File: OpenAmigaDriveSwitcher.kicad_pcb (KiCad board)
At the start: 2 copper layers, 21.8 x 57.7 mm, 6 parts, among them J1 SWITCH, J99 OSHW_LOGO, U1 74LS157, U8 EVEN_CIA_CHIP

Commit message: Ready for V1
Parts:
- added J2: SWITCH, OpenAmigaDriveSwitcher:SolderJumper3, F.Cu at (163.3, 106.7)
- J1: footprint OpenAmigaDriveSwitcher:LoosePads-3 -> OpenAmigaDriveSwitcher:Pin_Header_Straight_1x03-ModSilkS
- moved J1 25.1 mm to (163.3, 134.6), turned to 0 degrees
- moved J99 0.77 mm to (150.7, 109.2), turned to 270 degrees
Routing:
- net GND: track 0.00 -> 101.8 mm, vias 0 -> 18
- net VCC: track 46.0 -> 96.1 mm
- net Net-(J1-Pad2): track 28.4 -> 57.9 mm
- net Net-(U1-Pad2): track 16.2 -> 15.3 mm
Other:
- board size 21.8 x 57.7 mm -> 25.1 x 52.3 mm
- net class Power: via_dia 0.6 -> 0.8; via_drill 0.4 -> 0.6
- board text added: "NORMAL"
- board text added: "SWAP"
- board text added: "VCC|SWAP|GND"
- board text added: "github.com/SukkoPera/OpenAmigaDriveSwitcher"

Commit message: Add version number
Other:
- board text added: "V1"
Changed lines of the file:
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@@
     (links 59)
     (no_connects 0)
-    (area 134.62 96.36 178.03 170.086001)
+    (area 140.386999 102.032999 165.683001 154.507001)
     (thickness 1.6)
-    (drawings 23)
+    (drawings 24)
     (tracks 165)
     (zones 0)
@@
     )
   )
+  (gr_text V1 (at 164.084 104.013 90) (layer B.SilkS)
+    (effects (font (size 1 1) (thickness 0.15)) (justify mirror))
+  )
   (gr_text github.com/SukkoPera/OpenAmigaDriveSwitcher (at 151.13 132.842 90) (layer B.SilkS)

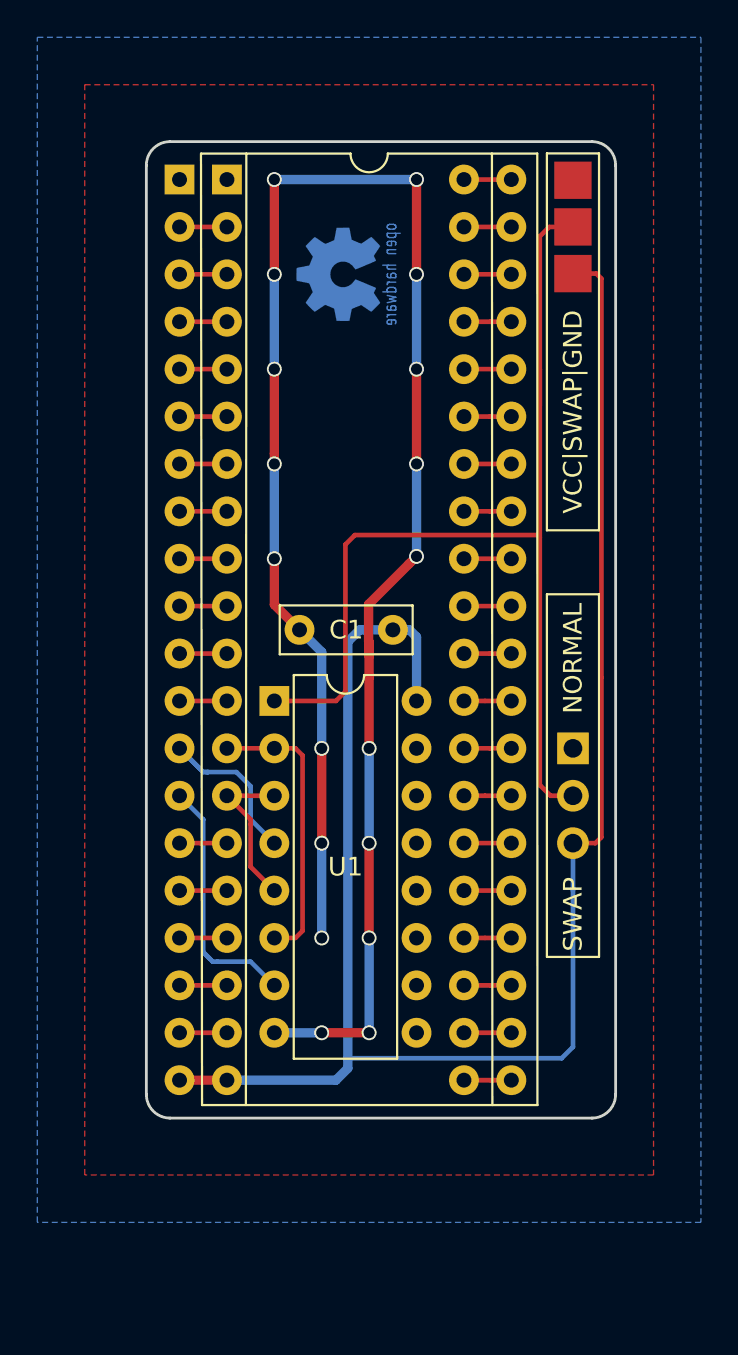
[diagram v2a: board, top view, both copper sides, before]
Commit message: V2: Reverse swap pin logic (i.e: swap drives when it is grounded) This will make the switcher more easily controllable by OpenAmigaMouseTrigger. Also migrate project to KiCad 5.
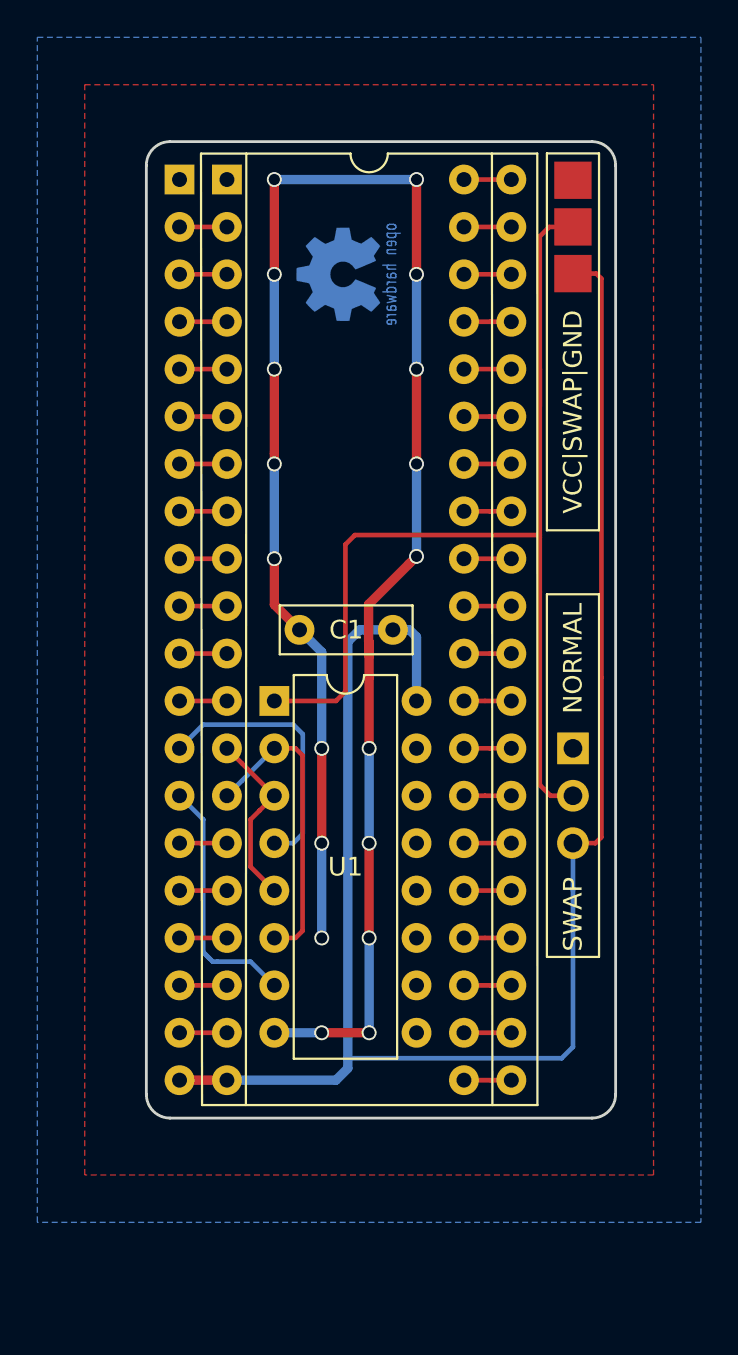
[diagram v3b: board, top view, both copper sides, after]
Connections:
- U8 pad 13: Net-(U1-Pad2) -> Net-(U1-Pad3)
- U8 pad 14: Net-(U1-Pad3) -> Net-(U1-Pad2)
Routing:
- net Net-(CONN1-Pad13): track 9.38 -> 14.4 mm
- net Net-(U1-Pad2): track 15.3 -> 16.3 mm
- net Net-(U1-Pad3): track 8.67 -> 9.72 mm
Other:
- board text added: "V2"
- board text removed: "V1"

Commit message: Remove legacy KiCad 4 symbols
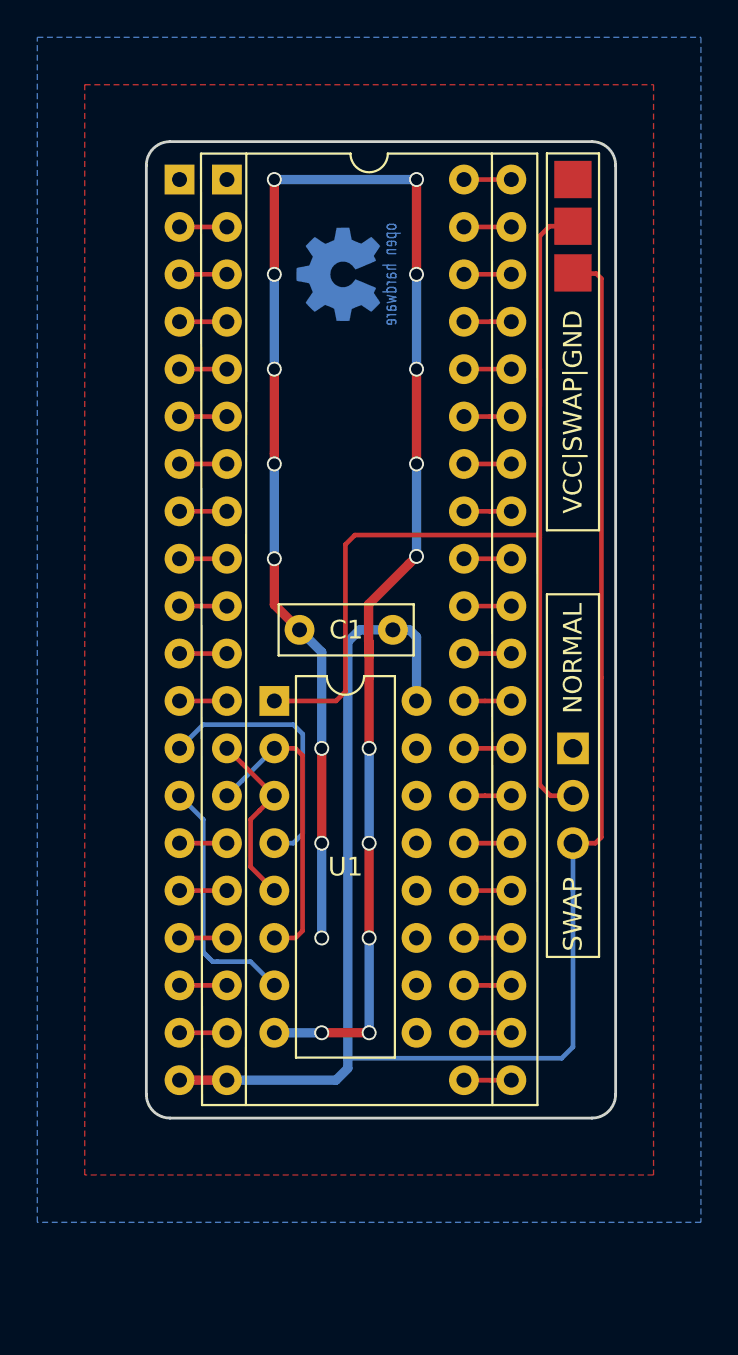
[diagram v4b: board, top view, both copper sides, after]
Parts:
- C1: value C -> 100n; footprint Capacitors_THT:C_Disc_D7.0mm_W2.5mm_P5.00mm -> Capacitor_THT:C_Disc_D7.0mm_W2.5mm_P5.00mm
- J1: value SWITCH -> PADS; footprint OpenAmigaDriveSwitcher:Pin_Header_Straight_1x03-ModSilkS -> OpenAmigaDriveSwitcher:SolderJumper3
- J2: footprint OpenAmigaDriveSwitcher:SolderJumper3 -> OpenAmigaDriveSwitcher:Pin_Header_Straight_1x03-ModSilkS
- U1: footprint Housings_DIP:DIP-16_W7.62mm -> Package_DIP:DIP-16_W7.62mm
- moved J1 28.0 mm to (163.3, 106.6), turned to 270 degrees
- moved J2 27.9 mm to (163.3, 134.6), turned to 0 degrees

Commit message: Fix and improve silkscreen
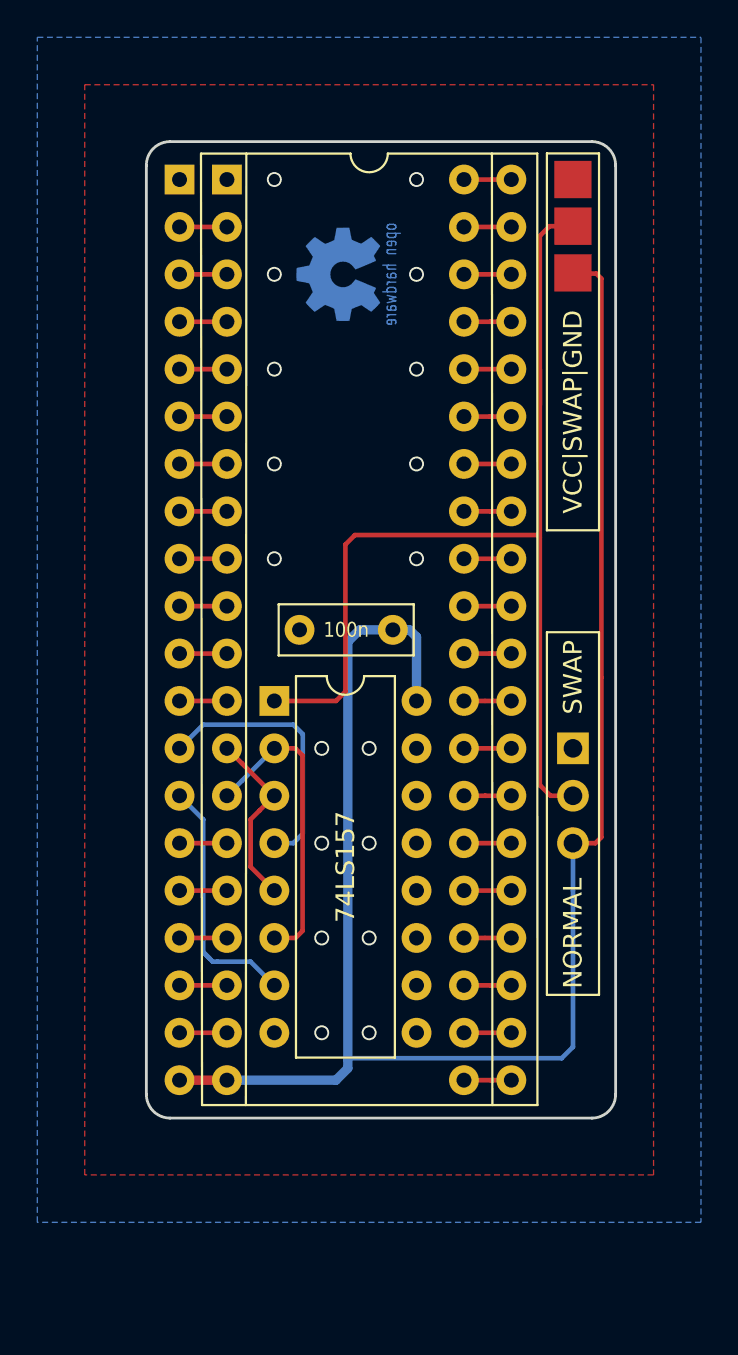
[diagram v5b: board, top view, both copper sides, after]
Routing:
- net GND: track 101.8 -> 0.00 mm
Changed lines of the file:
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@@
     (thickness 1.6)
     (drawings 24)
-    (tracks 161)
+    (tracks 131)
     (zones 0)
     (modules 7)
@@
     (descr "C, Disc series, Radial, pin pitch=5.00mm, , diameter*width=7*2.5mm^2, Capacitor, http://cdn-reichelt.de/documents/datenblatt/B300/DS_KERKO_TC.pdf")
     (tags "C Disc series Radial pin pitch 5.00mm  diameter 7mm width 2.5mm Capacitor")
-    (fp_text reference C1 (at 2.5 0 180) (layer F.SilkS)
-      (effects (font (size 1 1) (thickness 0.15)))
-    )
-    (fp_text value 100n (at 2.5 2.56 180) (layer F.Fab)
-      (effects (font (size 1 1) (thickness 0.15)))
+    (fp_text reference C1 (at 2.5 0 180) (layer F.SilkS) hide
+      (effects (font (size 1 1) (thickness 0.15)))
+    )
+    (fp_text value 100n (at 2.5 0 180) (layer F.SilkS)
+      (effects (font (size 0.8 0.7) (thickness 0.1)))
     )
     (fp_line (start -1 -1.25) (end -1 1.25) (layer F.Fab) (width 0.1))
@@
     (descr "16-lead though-hole mounted DIP package, row spacing 7.62 mm (300 mils)")
     (tags "THT DIP DIL PDIP 2.54mm 7.62mm 300mil")
-    (fp_text reference U1 (at 3.81 8.89) (layer F.SilkS)
-      (effects (font (size 1 1) (thickness 0.15)))
-    )
-    (fp_text value 74LS157 (at 3.81 20.17) (layer F.Fab)
+    (fp_text reference U1 (at 3.81 8.89) (layer F.SilkS) hide
+      (effects (font (size 1 1) (thickness 0.15)))
+    )
+    (fp_text value 74LS157 (at 3.81 8.89 90) (layer F.SilkS)
       (effects (font (size 1 1) (thickness 0.15)))
     )
@@
     (effects (font (size 1 1) (thickness 0.15)) (justify mirror))
   )
-  (gr_line (start 164.719 126.365) (end 164.719 145.796) (layer F.SilkS) (width 0.12))
-  (gr_line (start 161.925 145.796) (end 161.925 126.365) (layer F.SilkS) (width 0.12))
-  (gr_line (start 161.925 145.796) (end 164.719 145.796) (layer F.SilkS) (width 0.12))
-  (gr_line (start 161.925 126.365) (end 164.719 126.365) (layer F.SilkS) (width 0.12))
+  (gr_line (start 164.719 128.397) (end 164.719 147.828) (layer F.SilkS) (width 0.12))
+  (gr_line (start 161.925 147.828) (end 161.925 128.397) (layer F.SilkS) (width 0.12))
+  (gr_line (start 161.925 147.828) (end 164.719 147.828) (layer F.SilkS) (width 0.12))
+  (gr_line (start 161.925 128.397) (end 164.719 128.397) (layer F.SilkS) (width 0.12))
   (gr_line (start 161.925 122.936) (end 164.719 122.936) (layer F.SilkS) (width 0.12))
   (gr_line (start 161.925 102.743) (end 164.719 102.743) (layer F.SilkS) (width 0.12))
@@
     (effects (font (size 1 1) (thickness 0.15)))
   )
-  (gr_text NORMAL (at 163.322 129.794 90) (layer F.SilkS)
+  (gr_text NORMAL (at 163.322 144.526 90) (layer F.SilkS)
     (effects (font (size 1 1) (thickness 0.15)))
   )
-  (gr_text SWAP (at 163.322 143.51 90) (layer F.SilkS)
+  (gr_text SWAP (at 163.322 130.81 90) (layer F.SilkS)
     (effects (font (size 1 1) (thickness 0.15)))
   )
@@
   (gr_line (start 165.608 103.378) (end 165.608 153.162) (layer Edge.Cuts) (width 0.15))
   (gr_line (start 141.732 102.108) (end 164.338 102.108) (layer Edge.Cuts) (width 0.15))
+  (via (at 147.32 104.14) (size 0.8) (drill 0.6) (layers F.Cu B.Cu) (net 2))
   (segment (start 151.257 151.765) (end 151.257 151.257) (width 0.5) (layer B.Cu) (net 1))
   (segment (start 151.257 151.257) (end 151.257 128.905) (width 0.5) (layer B.Cu) (net 1))
@@
   (segment (start 164.572 109.18) (end 164.846 109.454) (width 0.25) (layer F.Cu) (net 1))
   (segment (start 142.24 152.4) (end 144.78 152.4) (width 0.5) (layer F.Cu) (net 1) (status 30))
-  (segment (start 147.32 124.46) (end 147.32 126.92) (width 0.5) (layer F.Cu) (net 2))
-  (segment (start 147.32 126.92) (end 148.67 128.27) (width 0.5) (layer F.Cu) (net 2) (status 20))
-  (segment (start 149.86 134.62) (end 149.86 129.46) (width 0.5) (layer B.Cu) (net 2))
-  (segment (start 149.86 129.46) (end 148.67 128.27) (width 0.5) (layer B.Cu) (net 2) (status 20))
-  (segment (start 147.32 119.38) (end 147.32 118.814315) (width 0.5) (layer F.Cu) (net 2))
-  (segment (start 147.32 118.814315) (end 147.32 114.3) (width 0.5) (layer F.Cu) (net 2))
-  (segment (start 147.32 124.46) (end 147.32 119.38) (width 0.5) (layer B.Cu) (net 2))
-  (via (at 147.32 119.38) (size 0.8) (drill 0.6) (layers F.Cu B.Cu) (net 2))
   (via (at 147.32 124.46) (size 0.8) (drill 0.6) (layers F.Cu B.Cu) (net 2))
-  (segment (start 152.4 129.667) (end 152.4 128.924002) (width 0.5) (layer F.Cu) (net 2))
-  (segment (start 152.4 128.924002) (end 152.369999 128.894001) (width 0.5) (layer F.Cu) (net 2))
-  (segment (start 152.369999 128.894001) (end 152.369999 126.903001) (width 0.5) (layer F.Cu) (net 2))
-  (segment (start 152.369999 126.903001) (end 154.540001 124.732999) (width 0.5) (layer F.Cu) (net 2))
-  (segment (start 154.540001 124.732999) (end 154.94 124.333) (width 0.5) (layer F.Cu) (net 2))
-  (segment (start 154.94 119.38) (end 154.94 124.333) (width 0.5) (layer B.Cu) (net 2))
-  (via (at 154.94 124.333) (size 0.8) (drill 0.6) (layers F.Cu B.Cu) (net 2))
-  (segment (start 154.94 114.3) (end 154.94 119.38) (width 0.5) (layer F.Cu) (net 2))
-  (via (at 154.94 119.38) (size 0.8) (drill 0.6) (layers F.Cu B.Cu) (net 2))
-  (segment (start 154.94 109.22) (end 154.94 114.3) (width 0.5) (layer B.Cu) (net 2))
-  (via (at 154.94 114.3) (size 0.8) (drill 0.6) (layers F.Cu B.Cu) (net 2))
-  (segment (start 154.94 104.14) (end 154.94 109.22) (width 0.5) (layer F.Cu) (net 2))
-  (via (at 154.94 109.22) (size 0.8) (drill 0.6) (layers F.Cu B.Cu) (net 2))
-  (segment (start 147.32 104.14) (end 154.94 104.14) (width 0.5) (layer B.Cu) (net 2))
-  (via (at 154.94 104.14) (size 0.8) (drill 0.6) (layers F.Cu B.Cu) (net 2))
-  (segment (start 147.32 109.22) (end 147.32 104.14) (width 0.5) (layer F.Cu) (net 2))
-  (via (at 147.32 104.14) (size 0.8) (drill 0.6) (layers F.Cu B.Cu) (net 2))
-  (segment (start 147.32 114.3) (end 147.32 109.22) (width 0.5) (layer B.Cu) (net 2))
-  (via (at 147.32 109.22) (size 0.8) (drill 0.6) (layers F.Cu B.Cu) (net 2))
-  (via (at 147.32 114.3) (size 0.8) (drill 0.6) (layers F.Cu B.Cu) (net 2))
-  (segment (start 152.4 129.101315) (end 152.4 129.667) (width 0.5) (layer F.Cu) (net 2))
-  (segment (start 152.369999 129.071314) (end 152.4 129.101315) (width 0.5) (layer F.Cu) (net 2))
-  (segment (start 152.4 130.81) (end 152.4 129.667) (width 0.5) (layer F.Cu) (net 2))
+  (via (at 149.86 149.86) (size 0.8) (drill 0.6) (layers F.Cu B.Cu) (net 2))
+  (via (at 152.4 149.86) (size 0.8) (drill 0.6) (layers F.Cu B.Cu) (net 2))
+  (via (at 152.4 139.7) (size 0.8) (drill 0.6) (layers F.Cu B.Cu) (net 2))
+  (via (at 152.4 134.62) (size 0.8) (drill 0.6) (layers F.Cu B.Cu) (net 2))
   (via (at 149.86 144.78) (size 0.8) (drill 0.6) (layers F.Cu B.Cu) (net 2))
-  (segment (start 149.86 139.7) (end 149.86 144.78) (width 0.5) (layer B.Cu) (net 2))
-  (segment (start 149.86 134.62) (end 149.86 139.7) (width 0.5) (layer F.Cu) (net 2))
   (via (at 149.86 139.7) (size 0.8) (drill 0.6) (layers F.Cu B.Cu) (net 2))
   (via (at 149.86 134.62) (size 0.8) (drill 0.6) (layers F.Cu B.Cu) (net 2))
-  (segment (start 152.4 134.62) (end 152.4 130.81) (width 0.5) (layer F.Cu) (net 2))
-  (segment (start 152.4 139.7) (end 152.4 134.62) (width 0.5) (layer B.Cu) (net 2))
-  (via (at 152.4 134.62) (size 0.8) (drill 0.6) (layers F.Cu B.Cu) (net 2))
-  (segment (start 152.4 144.78) (end 152.4 139.7) (width 0.5) (layer F.Cu) (net 2))
-  (via (at 152.4 139.7) (size 0.8) (drill 0.6) (layers F.Cu B.Cu) (net 2))
-  (segment (start 152.4 149.86) (end 152.4 144.78) (width 0.5) (layer B.Cu) (net 2))
+  (via (at 154.94 104.14) (size 0.8) (drill 0.6) (layers F.Cu B.Cu) (net 2))
+  (via (at 154.94 109.22) (size 0.8) (drill 0.6) (layers F.Cu B.Cu) (net 2))
+  (via (at 154.94 114.3) (size 0.8) (drill 0.6) (layers F.Cu B.Cu) (net 2))
+  (via (at 154.94 119.38) (size 0.8) (drill 0.6) (layers F.Cu B.Cu) (net 2))
+  (via (at 154.94 124.46) (size 0.8) (drill 0.6) (layers F.Cu B.Cu) (net 2))
+  (via (at 147.32 114.3) (size 0.8) (drill 0.6) (layers F.Cu B.Cu) (net 2))
+  (via (at 147.32 119.38) (size 0.8) (drill 0.6) (layers F.Cu B.Cu) (net 2))
+  (via (at 147.32 109.22) (size 0.8) (drill 0.6) (layers F.Cu B.Cu) (net 2))
   (via (at 152.4 144.78) (size 0.8) (drill 0.6) (layers F.Cu B.Cu) (net 2))
-  (segment (start 149.86 149.86) (end 152.4 149.86) (width 0.5) (layer F.Cu) (net 2))
-  (via (at 152.4 149.86) (size 0.8) (drill 0.6) (layers F.Cu B.Cu) (net 2))
-  (segment (start 147.32 149.86) (end 149.86 149.86) (width 0.5) (layer B.Cu) (net 2) (status 10))
-  (via (at 149.86 149.86) (size 0.8) (drill 0.6) (layers F.Cu B.Cu) (net 2))
   (segment (start 157.48 149.86) (end 160.02 149.86) (width 0.25) (layer F.Cu) (net 3) (status 30))
   (segment (start 142.24 106.68) (end 144.78 106.68) (width 0.25) (layer F.Cu) (net 4) (status 30))
